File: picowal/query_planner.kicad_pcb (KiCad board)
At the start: 4 copper layers, 130 x 80 mm, 29 parts, among them J1 UP, J2 DN, J3 UART, J4 SWD_QRY, J5 RJ45, J6 SWD_IDX, J7 NVMe_0, J8 NVMe_1, J9 NVMe_2, U1 ECP5-5G-45F, U10 TPS62A02_CORE, U11 RP2354B_IDX, U12 PSRAM_IDX, U13 RTL8221B, U14 W25Q128_IDX, U15 TPS62A01_IDX, U16 TPS54331_NVMe, U17 TPS23753A_PoE, U2 RP2354B_QRY, U3 SRAM_A, U4 SRAM_B, U5 PSRAM_QRY, U6 W25Q128_QRY, U7 W25Q128_CFG, U8 TPS62A01_QRY, U9 AP2112K_3V3, Y1 12MHz, Y2 25MHz, Y3 100MHz

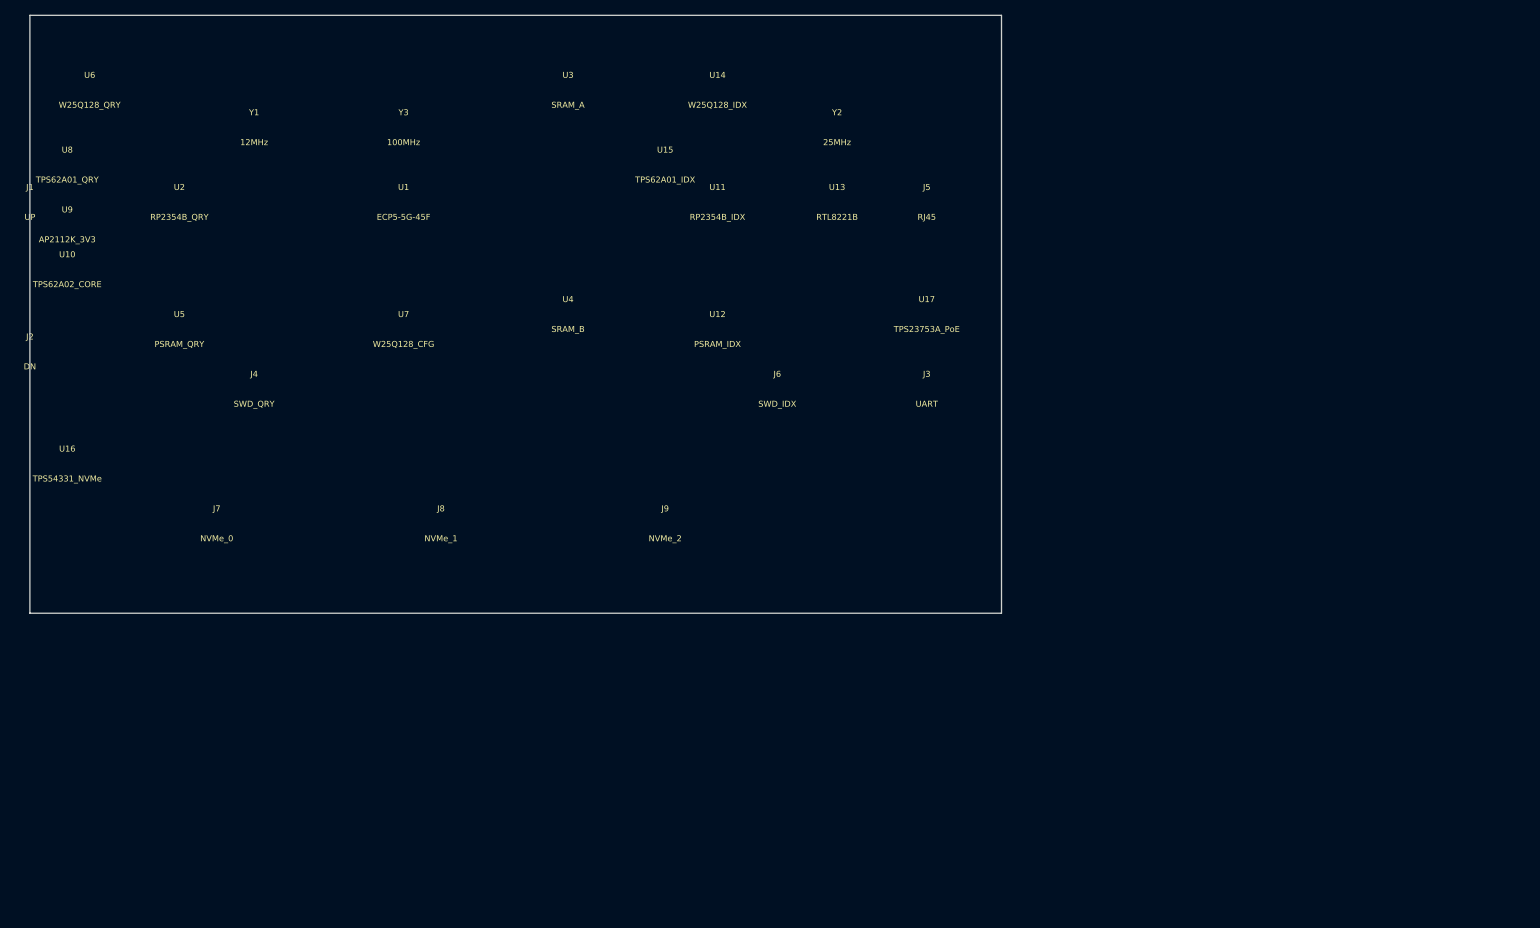
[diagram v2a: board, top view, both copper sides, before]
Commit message: Dual ECP5-85F: 2x2.5GbE + 5xNVMe + tile chain + 312 DSP MACs
Architecture upgrade to dual-FPGA insanity board:

  FPGA A (Network + Data):
    CH0 -> NVMe slot 0 (data shard)
    CH1 -> NVMe slot 1 (data shard)
    CH2 -> 2500BASE-X -> RTL8221B -> RJ45 PoE port A
    CH3 -> 2500BASE-X -> RTL8221B -> RJ45 PoE port B

  FPGA B (Storage + Chain):
    CH0 -> NVMe slot 2 (data shard)
    CH1 -> NVMe slot 3 (WAL - write-ahead log)
    CH2 -> NVMe slot 4 (indexes)
    CH3 -> Tile chain (SerDes link to next PicoWAL card)

Key specs:
  - 2x ECP5-5G-85F: 170K LUTs, 312 DSP MACs (62.4 GMAC/s INT18)
  - 5x M.2 NVMe: 3 data + 1 WAL + 1 index (~1.25 GB/s aggregate)
  - 2x 2.5GbE: 5 Gbps aggregate, dual TOE, dual PoE (51W budget)
  - Tile chain: cards daisy-chain via SerDes for distributed queries
  - Pin budget: FPGA A 120/205, FPGA B 67/205 (both comfortable)
  - Power: 22.9W total, 51W available (28W margin)
  - Board: 180x110mm, 4-layer
  - BOM: ~£99 (excl. NVMe SSDs)

Co-authored-by: Copilot <223556219+Copilot@users.noreply.github.com>
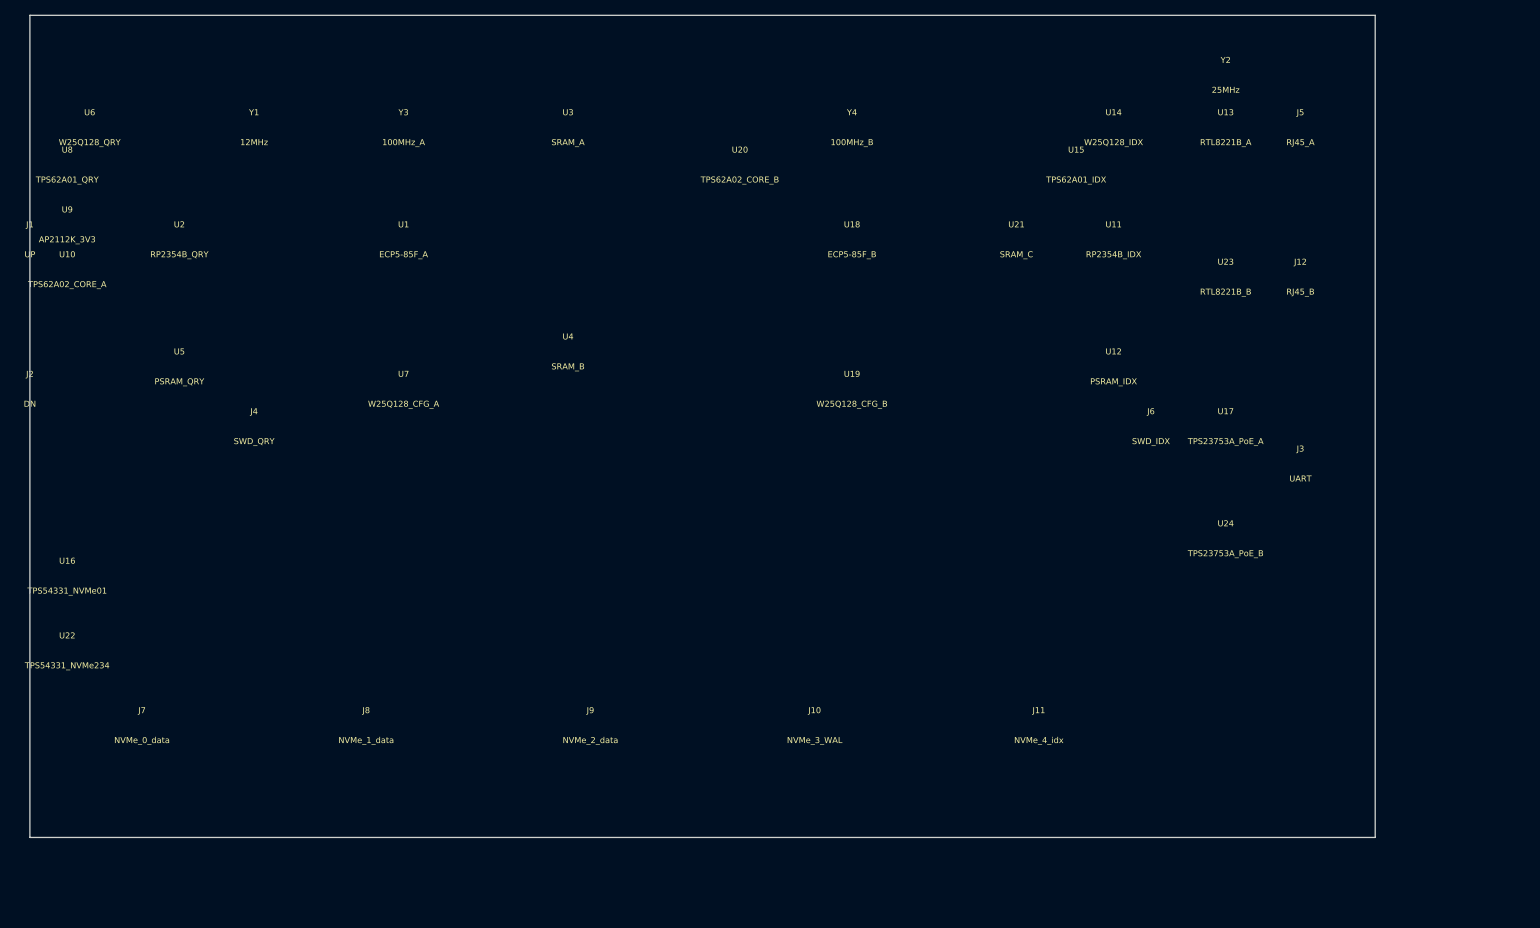
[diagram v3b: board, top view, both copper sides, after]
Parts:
- added J1: UP, Connector_PinHeader_2.54mm:PinHeader_2x10_P2.54mm_Vertical, F.Cu at (0.00, 30.0)
- added J12: RJ45_B, Connector_RJ45:RJ45_Amphenol_ARJM11C7, F.Cu at (170.0, 35.0)
- added J2: DN, Connector_PinHeader_2.54mm:PinHeader_2x10_P2.54mm_Vertical, F.Cu at (0.00, 50.0)
- added J3: UART, Connector_PinHeader_2.54mm:PinHeader_1x04_P2.54mm_Vertical, F.Cu at (170.0, 60.0)
- added J4: SWD_QRY, Connector_PinHeader_1.27mm:PinHeader_1x05_P1.27mm_Vertical, F.Cu at (30.0, 55.0)
- added J5: RJ45_A, Connector_RJ45:RJ45_Amphenol_ARJM11C7, F.Cu at (170.0, 15.0)
- added J6: SWD_IDX, Connector_PinHeader_1.27mm:PinHeader_1x05_P1.27mm_Vertical, F.Cu at (150.0, 55.0)
- added Y1: 12MHz, Crystal:Crystal_SMD_3215-2Pin_3.2x1.5mm, F.Cu at (30.0, 15.0)
- added Y2: 25MHz, Crystal:Crystal_SMD_3215-2Pin_3.2x1.5mm, F.Cu at (160.0, 8.00)
- added Y3: 100MHz_A, Oscillator:Oscillator_SMD_3225-4Pin_3.2x2.5mm, F.Cu at (50.0, 15.0)
- added Y4: 100MHz_B, Oscillator:Oscillator_SMD_3225-4Pin_3.2x2.5mm, F.Cu at (110.0, 15.0)
- J10: renamed from J5; value RJ45 -> NVMe_3_WAL; footprint Connector_RJ45:RJ45_Amphenol_ARJM11C7 -> Connector_M2:M2_M_Key_22x80
- J11: renamed from J6; value SWD_IDX -> NVMe_4_idx; footprint Connector_PinHeader_1.27mm:PinHeader_1x05_P1.27mm_Vertical -> Connector_M2:M2_M_Key_22x80
- J7: renamed from J2; value DN -> NVMe_0_data; footprint Connector_PinHeader_2.54mm:PinHeader_2x10_P2.54mm_Vertical -> Connector_M2:M2_M_Key_22x80
- J8: renamed from J3; value UART -> NVMe_1_data; footprint Connector_PinHeader_2.54mm:PinHeader_1x04_P2.54mm_Vertical -> Connector_M2:M2_M_Key_22x80
- J9: renamed from J4; value SWD_QRY -> NVMe_2_data; footprint Connector_PinHeader_1.27mm:PinHeader_1x05_P1.27mm_Vertical -> Connector_M2:M2_M_Key_22x80
- U1: value ECP5-5G-45F -> ECP5-85F_A
- U10: value TPS62A02_CORE -> TPS62A02_CORE_A
- U11: renamed from U15; value TPS62A01_IDX -> RP2354B_IDX; footprint Package_TO_SOT_SMD:SOT-23-6 -> Package_DFN_QFN:QFN-80-1EP_10x10mm_P0.4mm_EP5.45x5.45mm
- U12: renamed from U16; value TPS54331_NVMe -> PSRAM_IDX; footprint Package_SO:SOIC-8_3.9x4.9mm_P1.27mm -> Package_SO:SOP-8_3.9x4.9mm_P1.27mm
- U13: renamed from J8; value NVMe_1 -> RTL8221B_A; footprint Connector_M2:M2_M_Key_22x80 -> Package_DFN_QFN:QFN-56_7x7mm_P0.4mm
- U14: renamed from U17; value TPS23753A_PoE -> W25Q128_IDX; footprint Package_SO:TSSOP-20_4.4x6.5mm_P0.65mm -> Package_SO:SOIC-8_3.9x4.9mm_P1.27mm
- U15: renamed from J7; value NVMe_0 -> TPS62A01_IDX; footprint Connector_M2:M2_M_Key_22x80 -> Package_TO_SOT_SMD:SOT-23-6
- U16: renamed from Y3; value 100MHz -> TPS54331_NVMe01; footprint Oscillator:Oscillator_SMD_3225-4Pin_3.2x2.5mm -> Package_SO:SOIC-8_3.9x4.9mm_P1.27mm
- U17: renamed from Y1; value 12MHz -> TPS23753A_PoE_A; footprint Crystal:Crystal_SMD_3215-2Pin_3.2x1.5mm -> Package_SO:TSSOP-20_4.4x6.5mm_P0.65mm
- U18: renamed from U11; value RP2354B_IDX -> ECP5-85F_B; footprint Package_DFN_QFN:QFN-80-1EP_10x10mm_P0.4mm_EP5.45x5.45mm -> Package_BGA:BGA-381_17x17mm_P0.8mm
- U19: renamed from U12; value PSRAM_IDX -> W25Q128_CFG_B; footprint Package_SO:SOP-8_3.9x4.9mm_P1.27mm -> Package_SO:SOIC-8_3.9x4.9mm_P1.27mm
- U20: renamed from U13; value RTL8221B -> TPS62A02_CORE_B; footprint Package_DFN_QFN:QFN-56_7x7mm_P0.4mm -> Package_TO_SOT_SMD:SOT-23-6
- U21: renamed from U14; value W25Q128_IDX -> SRAM_C; footprint Package_SO:SOIC-8_3.9x4.9mm_P1.27mm -> Package_SO:TSOP-II-44_10.16x18.41mm_P0.8mm
- U22: renamed from J1; value UP -> TPS54331_NVMe234; footprint Connector_PinHeader_2.54mm:PinHeader_2x10_P2.54mm_Vertical -> Package_SO:SOIC-8_3.9x4.9mm_P1.27mm
- U23: renamed from J9; value NVMe_2 -> RTL8221B_B; footprint Connector_M2:M2_M_Key_22x80 -> Package_DFN_QFN:QFN-56_7x7mm_P0.4mm
- U24: renamed from Y2; value 25MHz -> TPS23753A_PoE_B; footprint Crystal:Crystal_SMD_3215-2Pin_3.2x1.5mm -> Package_SO:TSSOP-20_4.4x6.5mm_P0.65mm
- U7: value W25Q128_CFG -> W25Q128_CFG_A
- moved U12 140.6 mm to (145.0, 47.0)
- moved U17 136.0 mm to (160.0, 55.0)
- moved U15 124.6 mm to (140.0, 20.0)
- moved U13 117.6 mm to (160.0, 15.0)
- moved J8 87.5 mm to (45.0, 95.0)
- moved U23 81.9 mm to (160.0, 35.0)
- moved U24 75.7 mm to (160.0, 70.0)
- moved U16 75.0 mm to (5.00, 75.0)
- moved J10 71.6 mm to (105.0, 95.0)
- moved J9 63.6 mm to (75.0, 95.0)
- moved U11 60.8 mm to (145.0, 30.0)
- moved U22 60.2 mm to (5.00, 85.0)
- moved J11 57.0 mm to (135.0, 95.0)
- moved J7 52.2 mm to (15.0, 95.0)
- moved U21 44.7 mm to (132.0, 30.0)
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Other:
- board size 130 x 80 mm -> 180 x 110 mm

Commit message: 13x RP2354B uber config: 12 session + 1 index pico, CIFS/query/app roles
- 52 cores total (26x Cortex-M33 + 26x RISC-V Hazard3)
- Session picos are role-agnostic: CIFS/SMB2, SQL query, or app server
- FPGA A: 5 session picos (network-facing)
- FPGA B: 7 session + 1 index pico (storage-facing)
- Inter-FPGA 8-bit parallel GPIO link (11 pins each side)
- Pin budget: 183/205 on both FPGAs (OK)
- Power: 28W / 51W available (23W margin)
- Board cost: £113, full system with 5x 2TB NVMe: £593 (£407 under £1000)
- Board: 200x120mm, 4-layer
- PATH 5 added: CIFS/SMB2 via session pico

Co-authored-by: Copilot <223556219+Copilot@users.noreply.github.com>
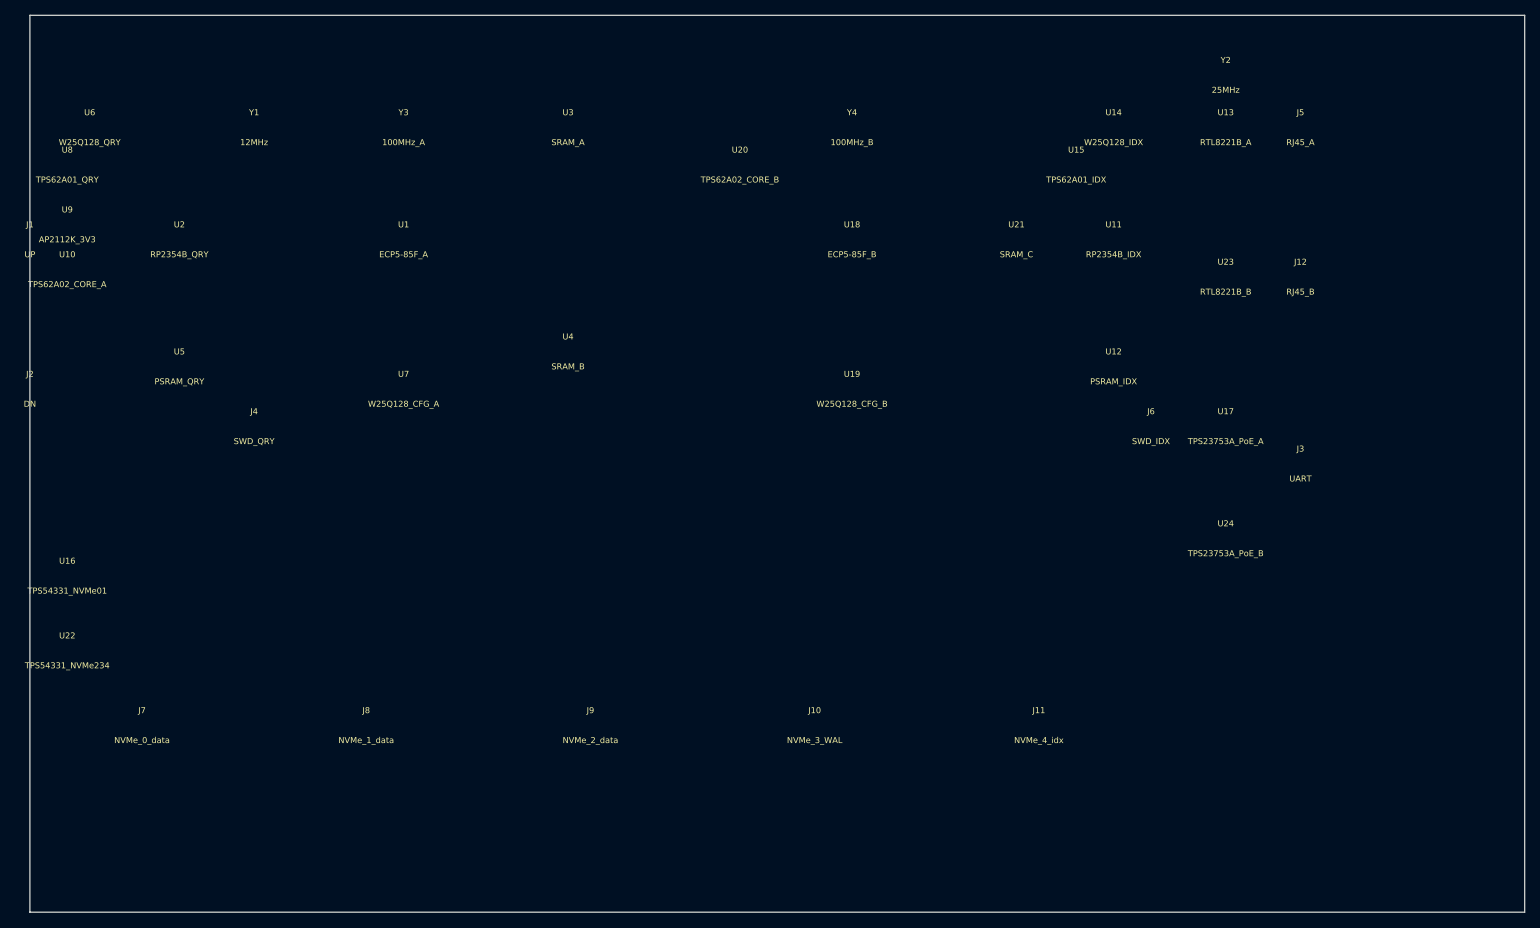
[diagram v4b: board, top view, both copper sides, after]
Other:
- board size 180 x 110 mm -> 200 x 120 mm
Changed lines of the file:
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@@
   (setup (grid_origin 0 0)
     (pcbplotparams (layerselection 0x00010fc_ffffffff) (outputdirectory "")))
-  (gr_rect (start 0 0) (end 180 110)
+  (gr_rect (start 0 0) (end 200 120)
     (stroke (width 0.1) (type default)) (fill none) (layer "Edge.Cuts"))
   (footprint "Package_BGA:BGA-381_17x17mm_P0.8mm"
